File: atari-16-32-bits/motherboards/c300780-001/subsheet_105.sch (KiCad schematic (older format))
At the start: 13 parts, among them J100 Power

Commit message: done u100,u101
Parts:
- removed C105, C106, C111, C112: 0.1uF, symbol Device:C
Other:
- note removed: "U100"
- note removed: "U101"
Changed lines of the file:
@@
 Collect power from PSU
-$Comp
-L Device:C C105
-U 1 1 607A3DD4
-P 1500 4150
-F 0 "C105" H 1525 4250 50  0000 L CNN
-F 1 "0.1uF" H 1525 4050 50  0000 L CNN
-F 2 "" H 1538 4000 50  0001 C CNN
-F 3 "~" H 1500 4150 50  0001 C CNN
-	1    1500 4150
-	1    0    0    -1
-$EndComp
-$Comp
-L Device:C C106
-U 1 1 607A4471
-P 2000 4150
-F 0 "C106" H 2025 4250 50  0000 L CNN
-F 1 "0.1uF" H 2025 4050 50  0000 L CNN
-F 2 "" H 2038 4000 50  0001 C CNN
-F 3 "~" H 2000 4150 50  0001 C CNN
-	1    2000 4150
-	1    0    0    -1
-$EndComp
 $Comp
 L Device:C C109
@@
 F 3 "~" H 3000 4150 50  0001 C CNN
 	1    3000 4150
-	1    0    0    -1
-$EndComp
-$Comp
-L Device:C C111
-U 1 1 607A4D3D
-P 4500 4150
-F 0 "C111" H 4525 4250 50  0000 L CNN
-F 1 "0.1uF" H 4525 4050 50  0000 L CNN
-F 2 "" H 4538 4000 50  0001 C CNN
-F 3 "~" H 4500 4150 50  0001 C CNN
-	1    4500 4150
-	1    0    0    -1
-$EndComp
-$Comp
-L Device:C C112
-U 1 1 607A519E
-P 5000 4150
-F 0 "C112" H 5025 4250 50  0000 L CNN
-F 1 "0.1uF" H 5025 4050 50  0000 L CNN
-F 2 "" H 5038 4000 50  0001 C CNN
-F 3 "~" H 5000 4150 50  0001 C CNN
-	1    5000 4150
 	1    0    0    -1
 $EndComp
@@
 	1    0    0    -1
 $EndComp
-Text Notes 1650 4700 0    50   ~ 0
-U101
 Text Notes 3150 4700 0    50   ~ 0
 J103
-Text Notes 4650 4700 0    50   ~ 0
-U100
 Text Notes 5700 4700 0    50   ~ 0
 U102
@@
 	1    0    0    -1
 $EndComp
-Text Label 1500 4300 3    50   ~ 0
-GND
-Text Label 2000 4300 3    50   ~ 0
-GND
 Text Label 3000 4300 3    50   ~ 0
 GND
 Text Label 3500 4300 3    50   ~ 0
-GND
-Text Label 4500 4300 3    50   ~ 0
-GND
-Text Label 5000 4300 3    50   ~ 0
 GND
 Text Label 5800 4300 3    50   ~ 0
@@
 Text Label 6700 4300 3    50   ~ 0
 GND
-Text Label 1500 4000 1    50   ~ 0
-VCC
-Text Label 2000 4000 1    50   ~ 0
-VCC
 Text Label 3000 4000 1    50   ~ 0
 VCC
 Text Label 3500 4000 1    50   ~ 0
 VCC
-Text Label 4500 4000 1    50   ~ 0
-VCC
-Text Label 5000 4000 1    50   ~ 0
-VCC
 Text Label 5800 4000 1    50   ~ 0

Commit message: done eprom
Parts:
- removed C113, C114: 0.1uF, symbol Device:C
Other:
- note removed: "U102"
- note removed: "U103"
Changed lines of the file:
@@
-$EndComp
-$Comp
-L Device:C C113
-U 1 1 607A54F5
-P 5800 4150
-F 0 "C113" H 5825 4250 50  0000 L CNN
-F 1 "0.1uF" H 5825 4050 50  0000 L CNN
-F 2 "" H 5838 4000 50  0001 C CNN
-F 3 "~" H 5800 4150 50  0001 C CNN
-	1    5800 4150
-	1    0    0    -1
-$EndComp
-$Comp
-L Device:C C114
-U 1 1 607A590E
-P 6700 4150
-F 0 "C114" H 6725 4250 50  0000 L CNN
-F 1 "0.1uF" H 6725 4050 50  0000 L CNN
-F 2 "" H 6738 4000 50  0001 C CNN
-F 3 "~" H 6700 4150 50  0001 C CNN
-	1    6700 4150
-	1    0    0    -1
 $EndComp
 $Comp
@@
 Text Notes 3150 4700 0    50   ~ 0
 J103
-Text Notes 5700 4700 0    50   ~ 0
-U102
-Text Notes 6600 4700 0    50   ~ 0
-U103
 Text Notes 3350 3500 0    100  ~ 0
 Bypass capacitors
@@
 Text Label 3500 4300 3    50   ~ 0
 GND
-Text Label 5800 4300 3    50   ~ 0
-GND
-Text Label 6700 4300 3    50   ~ 0
-GND
 Text Label 3000 4000 1    50   ~ 0
 VCC
 Text Label 3500 4000 1    50   ~ 0
 VCC
-Text Label 5800 4000 1    50   ~ 0
-VCC
-Text Label 6700 4000 1    50   ~ 0
-VCC
 $Comp

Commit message: sheet 1 done
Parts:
- removed C109: 0.1uF, symbol Device:C
- removed C110: 100uF, symbol Device:CP1
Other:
- note removed: "Bypass capacitors"
- note removed: "J103"
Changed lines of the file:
@@
 Collect power from PSU
-$Comp
-L Device:C C109
-U 1 1 607A48CD
-P 3000 4150
-F 0 "C109" H 3025 4250 50  0000 L CNN
-F 1 "0.1uF" H 3025 4050 50  0000 L CNN
-F 2 "" H 3038 4000 50  0001 C CNN
-F 3 "~" H 3000 4150 50  0001 C CNN
-	1    3000 4150
-	1    0    0    -1
-$EndComp
-$Comp
-L Device:CP1 C110
-U 1 1 607A6B48
-P 3500 4150
-F 0 "C110" H 3525 4250 50  0000 L CNN
-F 1 "100uF" H 3525 4050 50  0000 L CNN
-F 2 "" H 3500 4150 50  0001 C CNN
-F 3 "~" H 3500 4150 50  0001 C CNN
-	1    3500 4150
-	1    0    0    -1
-$EndComp
-Text Notes 3150 4700 0    50   ~ 0
-J103
-Text Notes 3350 3500 0    100  ~ 0
-Bypass capacitors
 $Comp
 L power:GND #PWR0103
@@
 	1    0    0    -1
 $EndComp
-Text Label 3000 4300 3    50   ~ 0
-GND
-Text Label 3500 4300 3    50   ~ 0
-GND
-Text Label 3000 4000 1    50   ~ 0
-VCC
-Text Label 3500 4000 1    50   ~ 0
-VCC
 $Comp
 L power:PWR_FLAG #FLG0101

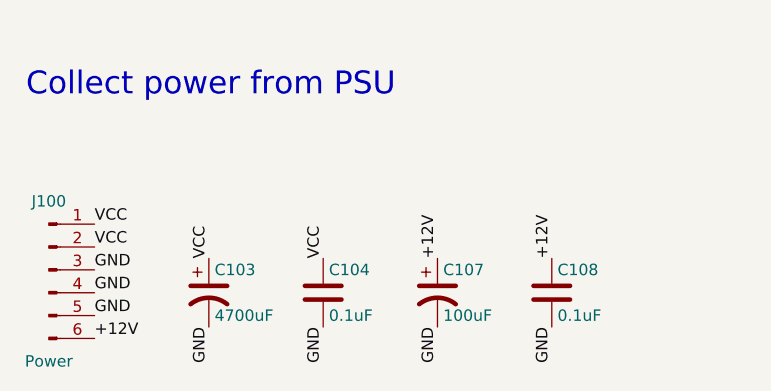
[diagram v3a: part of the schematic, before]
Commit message: reorganized sheets
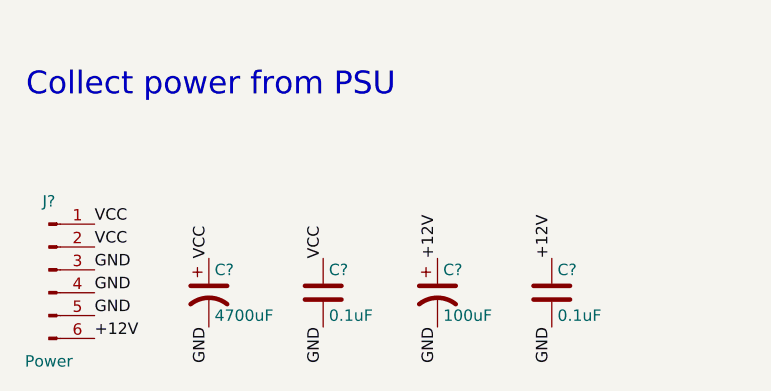
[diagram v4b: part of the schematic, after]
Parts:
- renumbered C103 to C?, C107 to C?, C104 to C?, C108 to C?, J100 to J?
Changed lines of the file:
@@
 $Descr A4 8268 11693 portrait
 encoding utf-8
-Sheet 8 14
+Sheet 12 8
 Title ""
 Date ""
@@
 $EndDescr
 $Comp
-L Connector:Conn_01x06_Male J100
+L Connector:Conn_01x06_Male J?
 U 1 1 607885AB
 P 1300 1900
-F 0 "J100" H 1300 2200 50  0000 C CNN
+F 0 "J?" H 1300 2200 50  0000 C CNN
 F 1 "Power" H 1300 1500 50  0000 C CNN
 F 2 "" H 1300 1900 50  0001 C CNN
@@
 $EndComp
 $Comp
-L Device:CP1 C103
+L Device:CP1 C?
 U 1 1 6079D92A
 P 2000 2000
-F 0 "C103" H 2025 2100 50  0000 L CNN
+F 0 "C?" H 2025 2100 50  0000 L CNN
 F 1 "4700uF" H 2025 1900 50  0000 L CNN
 F 2 "" H 2000 2000 50  0001 C CNN
@@
 $EndComp
 $Comp
-L Device:CP1 C107
+L Device:CP1 C?
 U 1 1 6079EFD5
 P 3000 2000
-F 0 "C107" H 3025 2100 50  0000 L CNN
+F 0 "C?" H 3025 2100 50  0000 L CNN
 F 1 "100uF" H 3025 1900 50  0000 L CNN
 F 2 "" H 3000 2000 50  0001 C CNN
@@
 $EndComp
 $Comp
-L Device:C C104
+L Device:C C?
 U 1 1 6079F96C
 P 2500 2000
-F 0 "C104" H 2525 2100 50  0000 L CNN
+F 0 "C?" H 2525 2100 50  0000 L CNN
 F 1 "0.1uF" H 2525 1900 50  0000 L CNN
 F 2 "" H 2538 1850 50  0001 C CNN
@@
 $EndComp
 $Comp
-L Device:C C108
+L Device:C C?
 U 1 1 6079FF6E
 P 3500 2000
-F 0 "C108" H 3525 2100 50  0000 L CNN
+F 0 "C?" H 3525 2100 50  0000 L CNN
 F 1 "0.1uF" H 3525 1900 50  0000 L CNN
 F 2 "" H 3538 1850 50  0001 C CNN
@@
 Collect power from PSU
 $Comp
-L power:GND #PWR0103
+L power:GND #PWR?
 U 1 1 607C25E0
 P 7300 2000
-F 0 "#PWR0103" H 7300 1750 50  0001 C CNN
+F 0 "#PWR?" H 7300 1750 50  0001 C CNN
 F 1 "GND" H 7300 1850 50  0000 C CNN
 F 2 "" H 7300 2000 50  0001 C CNN
@@
 $EndComp
 $Comp
-L power:PWR_FLAG #FLG0102
+L power:PWR_FLAG #FLG?
 U 1 1 607A7F7D
 P 7300 1000
-F 0 "#FLG0102" H 7300 1075 50  0001 C CNN
+F 0 "#FLG?" H 7300 1075 50  0001 C CNN
 F 1 "PWR_FLAG" H 7300 1150 50  0000 C CNN
 F 2 "" H 7300 1000 50  0001 C CNN
@@
 $EndComp
 $Comp
-L power:PWR_FLAG #FLG0103
+L power:PWR_FLAG #FLG?
 U 1 1 607A8CA9
 P 7300 1500
-F 0 "#FLG0103" H 7300 1575 50  0001 C CNN
+F 0 "#FLG?" H 7300 1575 50  0001 C CNN
 F 1 "PWR_FLAG" H 7300 1650 50  0000 C CNN
 F 2 "" H 7300 1500 50  0001 C CNN
@@
 $EndComp
 $Comp
-L power:VCC #PWR0101
+L power:VCC #PWR?
 U 1 1 607A923D
 P 7300 1000
-F 0 "#PWR0101" H 7300 850 50  0001 C CNN
+F 0 "#PWR?" H 7300 850 50  0001 C CNN
 F 1 "VCC" H 7300 1150 50  0000 C CNN
 F 2 "" H 7300 1000 50  0001 C CNN
@@
 $EndComp
 $Comp
-L power:+12V #PWR0102
+L power:+12V #PWR?
 U 1 1 607A9DD4
 P 7300 1500
-F 0 "#PWR0102" H 7300 1350 50  0001 C CNN
+F 0 "#PWR?" H 7300 1350 50  0001 C CNN
 F 1 "+12V" H 7300 1640 50  0000 C CNN
 F 2 "" H 7300 1500 50  0001 C CNN
@@
 $EndComp
 $Comp
-L power:PWR_FLAG #FLG0101
+L power:PWR_FLAG #FLG?
 U 1 1 607A87E9
 P 7300 2000
-F 0 "#FLG0101" H 7300 2075 50  0001 C CNN
+F 0 "#FLG?" H 7300 2075 50  0001 C CNN
 F 1 "PWR_FLAG" H 7300 2150 50  0000 C CNN
 F 2 "" H 7300 2000 50  0001 C CNN

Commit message: re-annotate component following move of subsheets in schematics
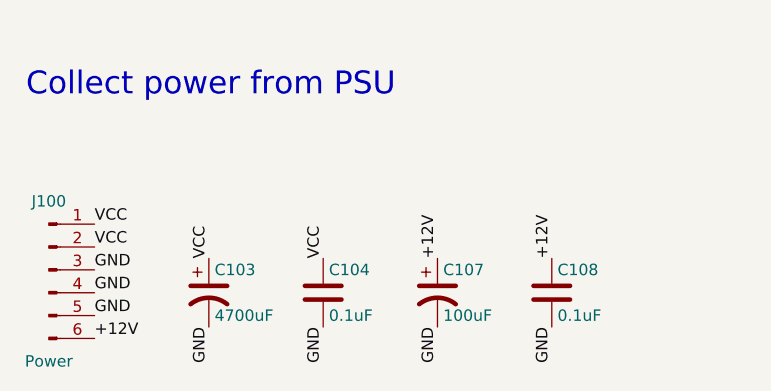
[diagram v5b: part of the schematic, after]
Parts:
- gave numbers to parts that had none: 5
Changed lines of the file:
@@
 $Descr A4 8268 11693 portrait
 encoding utf-8
-Sheet 12 8
+Sheet 6 9
 Title ""
 Date ""
@@
 $EndDescr
 $Comp
-L Connector:Conn_01x06_Male J?
+L Connector:Conn_01x06_Male J100
 U 1 1 607885AB
 P 1300 1900
-F 0 "J?" H 1300 2200 50  0000 C CNN
+F 0 "J100" H 1300 2200 50  0000 C CNN
 F 1 "Power" H 1300 1500 50  0000 C CNN
 F 2 "" H 1300 1900 50  0001 C CNN
@@
 $EndComp
 $Comp
-L Device:CP1 C?
+L Device:CP1 C103
 U 1 1 6079D92A
 P 2000 2000
-F 0 "C?" H 2025 2100 50  0000 L CNN
+F 0 "C103" H 2025 2100 50  0000 L CNN
 F 1 "4700uF" H 2025 1900 50  0000 L CNN
 F 2 "" H 2000 2000 50  0001 C CNN
@@
 $EndComp
 $Comp
-L Device:CP1 C?
+L Device:CP1 C107
 U 1 1 6079EFD5
 P 3000 2000
-F 0 "C?" H 3025 2100 50  0000 L CNN
+F 0 "C107" H 3025 2100 50  0000 L CNN
 F 1 "100uF" H 3025 1900 50  0000 L CNN
 F 2 "" H 3000 2000 50  0001 C CNN
@@
 $EndComp
 $Comp
-L Device:C C?
+L Device:C C104
 U 1 1 6079F96C
 P 2500 2000
-F 0 "C?" H 2525 2100 50  0000 L CNN
+F 0 "C104" H 2525 2100 50  0000 L CNN
 F 1 "0.1uF" H 2525 1900 50  0000 L CNN
 F 2 "" H 2538 1850 50  0001 C CNN
@@
 $EndComp
 $Comp
-L Device:C C?
+L Device:C C108
 U 1 1 6079FF6E
 P 3500 2000
-F 0 "C?" H 3525 2100 50  0000 L CNN
+F 0 "C108" H 3525 2100 50  0000 L CNN
 F 1 "0.1uF" H 3525 1900 50  0000 L CNN
 F 2 "" H 3538 1850 50  0001 C CNN
